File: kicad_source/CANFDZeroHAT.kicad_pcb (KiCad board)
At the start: 2 copper layers, 65 x 30 mm, 34 parts, among them CN1 RASPI-IO, CN2 691322310004, CN3 GH_SM04B-GHS-TB, CN4 GH_SM04B-GHS-TB, SW1 JS202011JCQN, U1 MCP2518FD, U2 TCAN332GDR, Y1 RH100-40.000-18-F-2050-TR

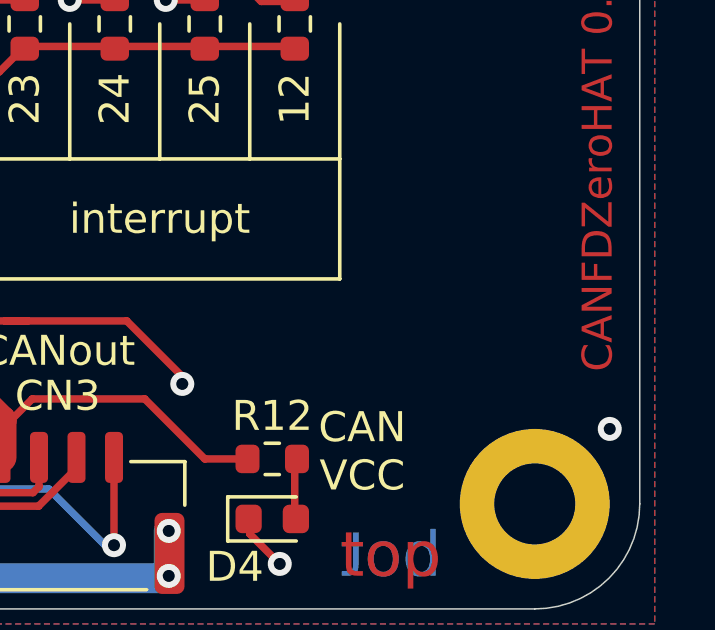
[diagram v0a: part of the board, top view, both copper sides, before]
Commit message: added cyphal logo
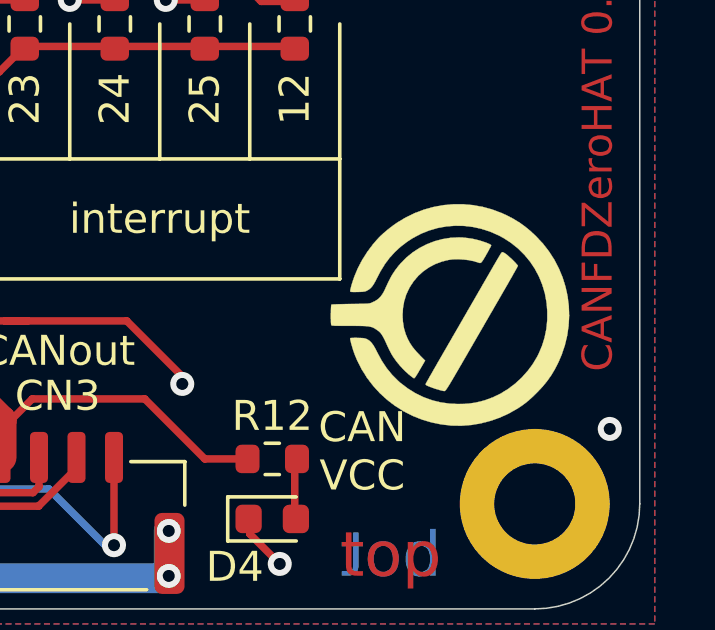
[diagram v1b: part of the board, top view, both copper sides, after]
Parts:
- added L4: Label, generationmake:opencyphal_small, F.Cu at (166.2, 106.7)
- CN3, CN4: value GH_SM04B-GHS-TB -> SM04B-GHS-TB
- D1: value DNI -> MBR0530T
- D2: value 150060GS75000 -> 19-217/GHC-YR1S2/3T
- D3: value 150060RS75000 -> KT-0603R
- D4: value 150060YS75000 -> 19-213/Y2C-CQ2R2L/3T(CY)
- R10, R11: value 1k -> 2k2
- R12: value 2k -> 10k
- U1: value MCP2518FD -> MCP2518FDT-E/SL

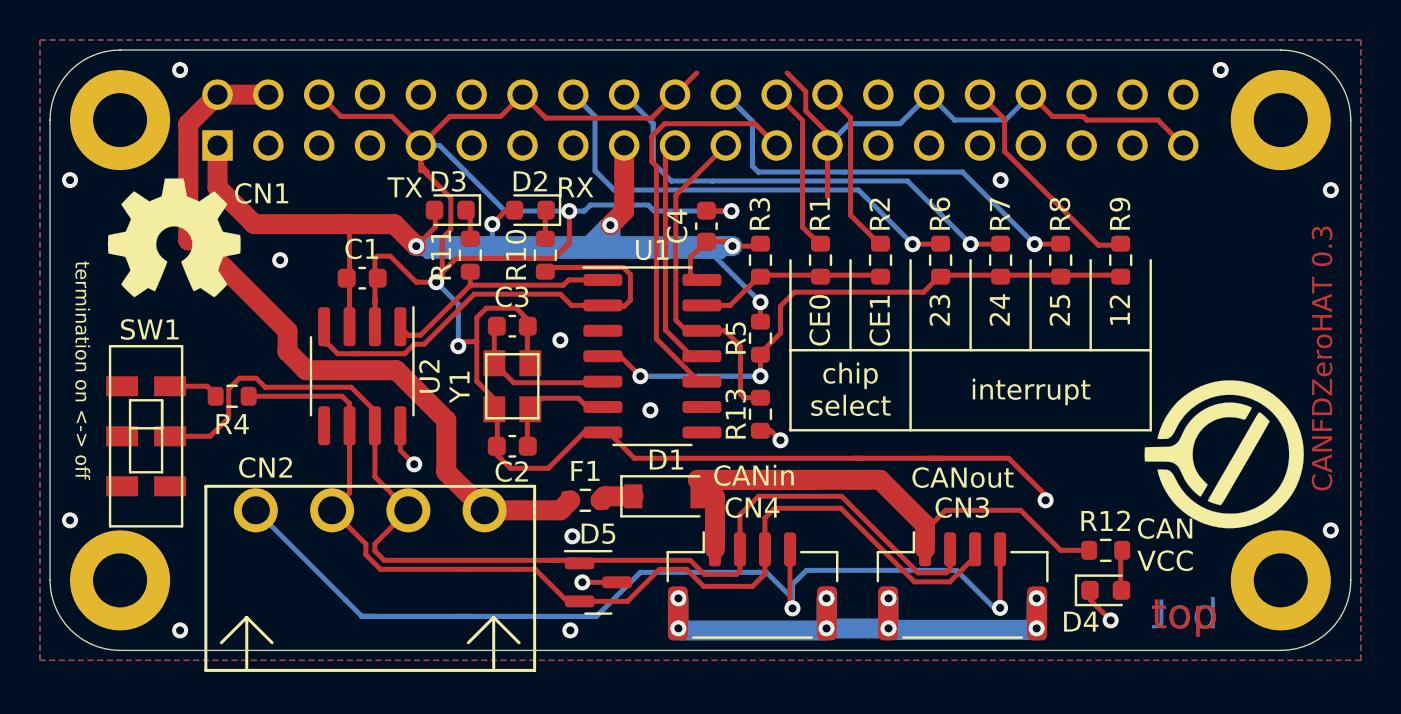
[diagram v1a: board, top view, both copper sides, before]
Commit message: updated some part numbers
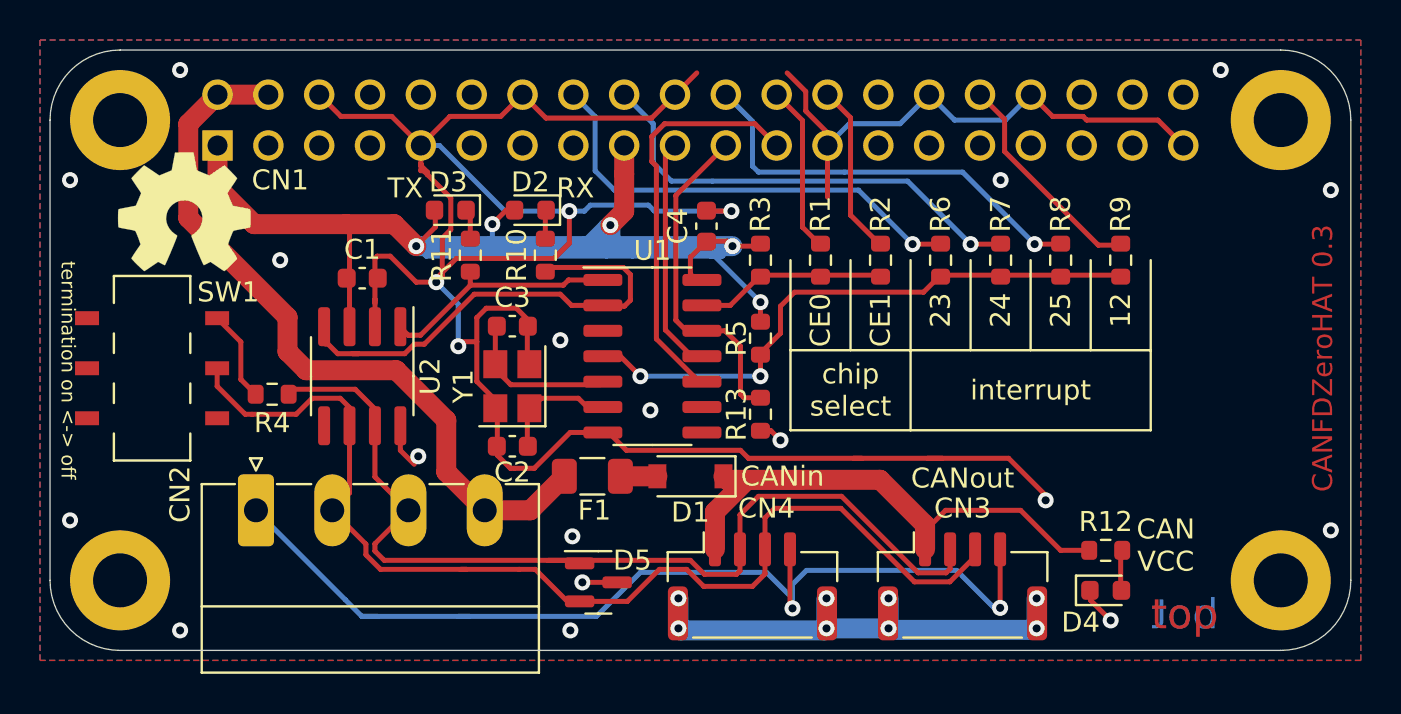
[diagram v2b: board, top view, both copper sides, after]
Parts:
- CN2: value 691322310004 -> XY2500R-F-3.81-4P; footprint CON_wuerth:WR-TBL_691322310004 -> Connector_Phoenix_MC:PhoenixContact_MC_1,5_4-G-3.81_1x04_P3.81mm_Horizontal
- F1: value 0ZCM0020FF2G -> nSMD050-33V; footprint Resistor_SMD:R_0603_1608Metric -> Fuse:Fuse_1206_3216Metric
- L4: moved to B.Cu
- SW1: value JS202011JCQN -> SS-3235S-L3; footprint mechanical-switches:CK_JS202011JCQN -> generationmake:SW_DPDT_XKB_SS-3235S-L3
- Y1: value RH100-40.000-18-F-2050-TR -> X1E0000210808; footprint crystals:Crystal_SMD_3.2x2.5mm_4Pad -> Crystal:Crystal_SMD_3225-4Pin_3.2x2.5mm
- moved L4 9.04 mm to (162.0, 98.7), turned to 180 degrees
- moved CN2 5.71 mm to (117.8, 109.5)
- moved SW1 3.41 mm to (112.6, 102.4)
- moved R4 2.00 mm to (118.6, 103.7)
- moved D1 1.56 mm to (139.5, 107.8), turned to 180 degrees
- moved L3 1.39 mm to (114.2, 94.6)
- moved F1 1.25 mm to (134.6, 107.8)
- turned Y1 to 90 degrees
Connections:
- D1 pad 1: /CANVCC_F -> /CANVCC
- D1 pad 2: /CANVCC -> /CANVCC_F
- R4 pad 1: /CANL -> /CANH
- SW1 pad 2: /CANH -> /CANL
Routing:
- net /CANVCC: track 43.9 -> 34.1 mm
- net /CANH: track 58.1 -> 50.1 mm
- net /CANL: track 52.3 -> 55.4 mm
- net Net-(R4-Pad2): track 2.56 -> 4.60 mm
- net GND: track 199.8 -> 200.8 mm

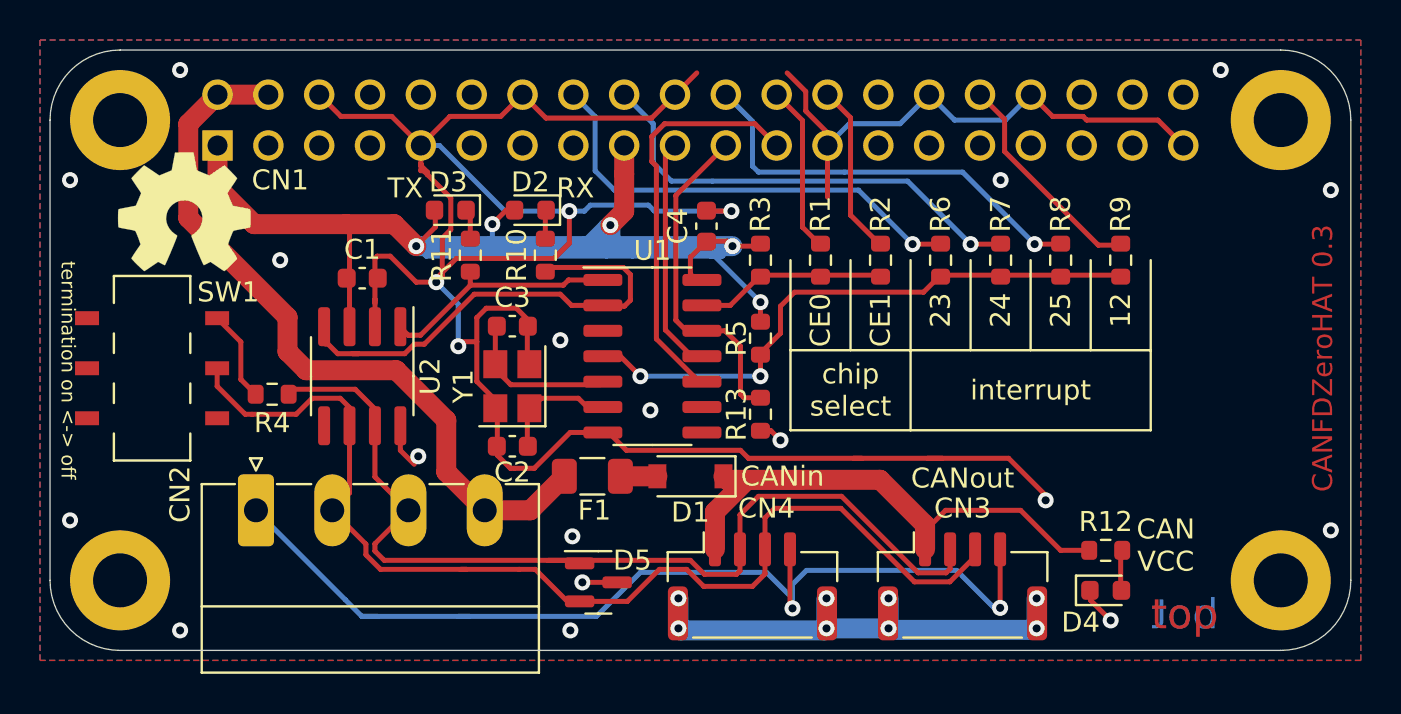
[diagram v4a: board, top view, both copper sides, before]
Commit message: fixed lirary errors and DRCs
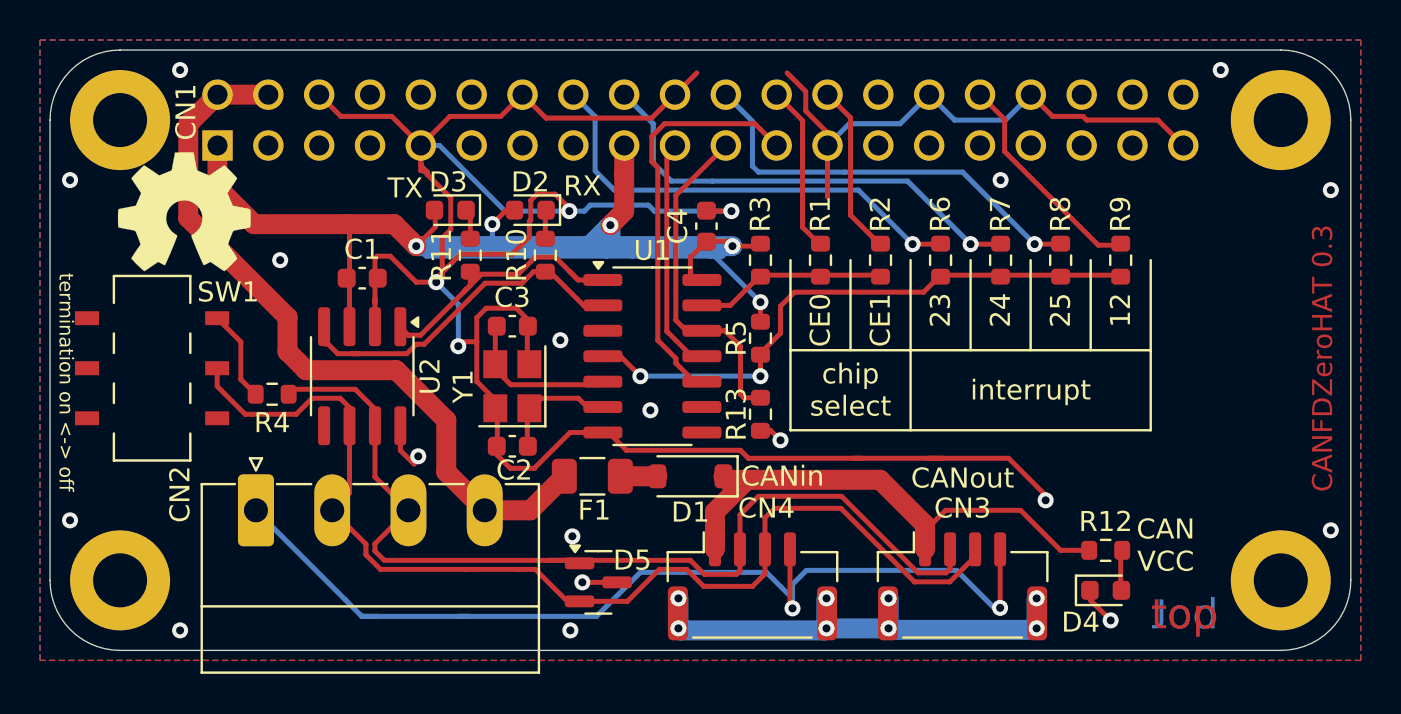
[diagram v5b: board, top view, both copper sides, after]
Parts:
- CN1: footprint MODULE_compute:RASPI_ZERO_HAT_EDGE -> generationmake:RASPI_ZERO_HAT_EDGE
- L1: footprint labels:generationmake_small_solder -> generationmake:generationmake_small_solder
- L2: footprint labels:generationmake_logo -> generationmake:generationmake_logo
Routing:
- net /CAN_RX: track 25.2 -> 18.9 mm
- net /CANVCC: track 34.1 -> 30.9 mm
- net /CAN_TX: track 12.0 -> 14.1 mm
- net GND: track 200.8 -> 201.6 mm
